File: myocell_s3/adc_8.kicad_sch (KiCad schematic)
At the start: 50 parts, among them U2 ADS1298xPAG

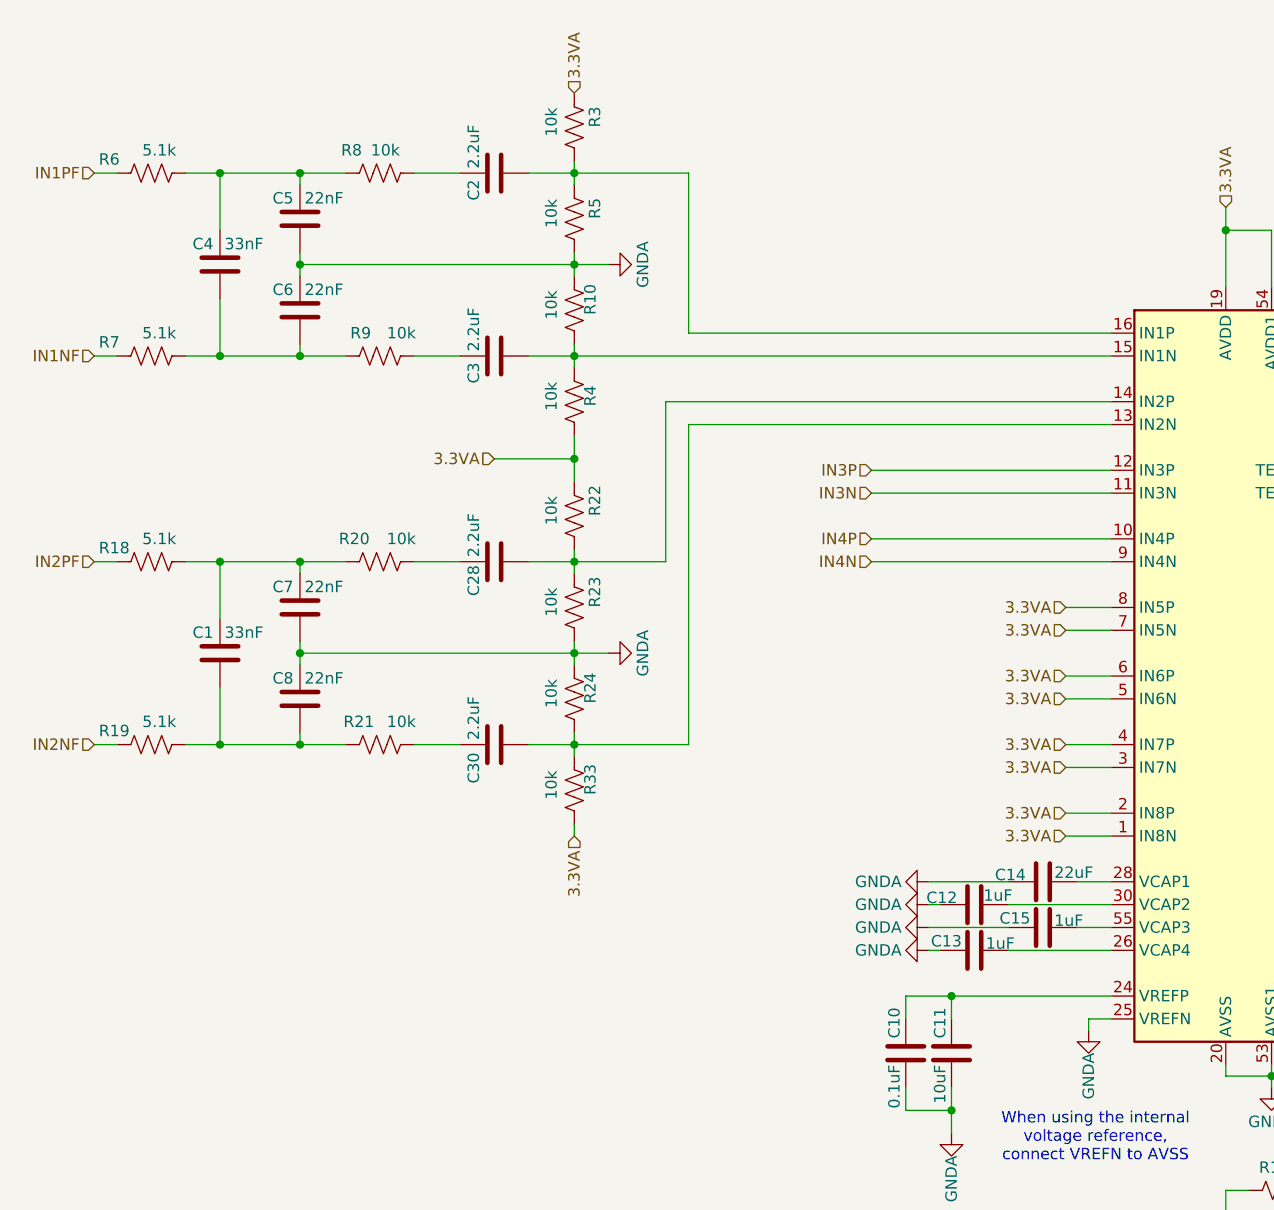
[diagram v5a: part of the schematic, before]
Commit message: schematic updated: channels 3,4 is onboard now
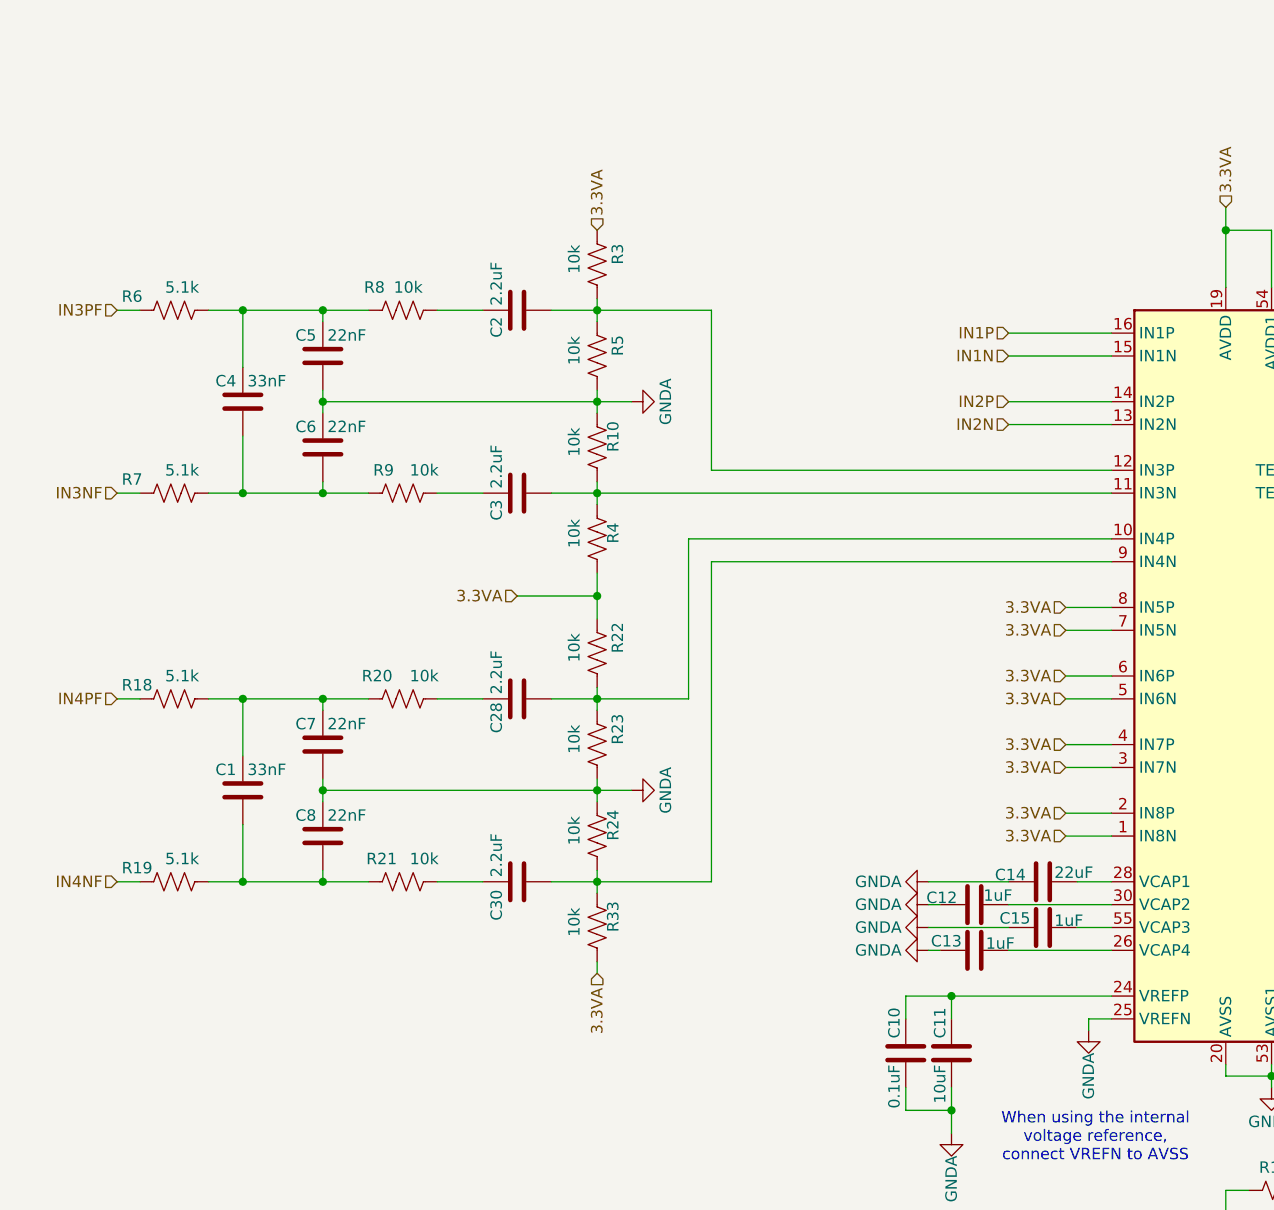
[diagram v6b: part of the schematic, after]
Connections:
- net IN3N is gone; now on an unnamed net: U2.11 (IN3N)
- net IN3P is gone; now on an unnamed net: U2.12 (IN3P)
- net IN4N is gone; now on an unnamed net: U2.9 (IN4N)
- net IN4P is gone; now on an unnamed net: U2.10 (IN4P)
- net at C3.2, R10.1, R4.2: no longer U2.15 (IN1N)
- net at C28.2, R22.1, R23.2: no longer U2.14 (IN2P)
- net at C2.2, R3.1, R5.2: no longer U2.16 (IN1P)
- net at C30.2, R24.1, R33.2: no longer U2.13 (IN2N)
- net IN1NF renamed IN3NF
- net IN1PF renamed IN3PF
- net IN2NF renamed IN4NF
- net IN2PF renamed IN4PF
- new net IN1N: U2.15 (IN1N)
- new net IN1P: U2.16 (IN1P)
- new net IN2N: U2.13 (IN2N)
- new net IN2P: U2.14 (IN2P)
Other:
- moved on the sheet: C1, C2, C28, C3, C30, C4, C5, C6, C7, C8, R10, R18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

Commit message: tracing analogue interfaces
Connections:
- net in3-: now reaches C3.2, R10.1, R4.2, U2.11 (IN3N)
- net in4+: now reaches C28.2, R22.1, R23.2, U2.10 (IN4P)
- net in3+: now reaches C2.2, R3.1, R5.2, U2.12 (IN3P)
- net in4-: now reaches C30.2, R24.1, R33.2, U2.9 (IN4N)
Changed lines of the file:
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@@
+		)
+	)
+	(label "in4+"
+		(at 115.57 73.66 0)
+		(effects
+			(font
+				(size 1.27 1.27)
+			)
+			(justify left bottom)
+		)
+	)
+	(label "in2-"
+		(at 135.89 60.96 0)
+		(effects
+			(font
+				(size 1.27 1.27)
+			)
+			(justify left bottom)
+		)
+	)
+	(label "in1-"
+		(at 135.89 53.34 0)
+		(effects
+			(font
+				(size 1.27 1.27)
+			)
+			(justify left bottom)
+		)
+	)
+	(label "in3+"
+		(at 115.57 66.04 0)
+		(effects
+			(font
+				(size 1.27 1.27)
+			)
+			(justify left bottom)
+		)
+	)
+	(label "in4-"
+		(at 115.57 76.2 0)
+		(effects
+			(font
+				(size 1.27 1.27)
+			)
+			(justify left bottom)
+		)
+	)
+	(label "in3-"
+		(at 115.57 68.58 0)
+		(effects
+			(font
+				(size 1.27 1.27)
+			)
+			(justify left bottom)
+		)
+	)
+	(label "in1+"
+		(at 135.89 50.8 0)
+		(effects
+			(font
+				(size 1.27 1.27)
+			)
+			(justify left bottom)
+		)
+	)
+	(label "in2+"
+		(at 135.89 58.42 0)
+		(effects
+			(font
+				(size 1.27 1.27)
+			)
+			(justify left bottom)
 		)
 	)

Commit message: tracing polygons
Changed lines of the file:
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@@
 	(wire
 		(pts
-			(xy 31.75 111.76) (xy 34.29 111.76)
+			(xy 25.4 111.76) (xy 34.29 111.76)
 		)
 		(stroke
@@
 	(wire
 		(pts
-			(xy 31.75 91.44) (xy 34.29 91.44)
+			(xy 25.4 91.44) (xy 34.29 91.44)
 		)
 		(stroke
@@
 	(wire
 		(pts
-			(xy 31.75 48.26) (xy 34.29 48.26)
+			(xy 24.13 48.26) (xy 34.29 48.26)
 		)
 		(stroke
@@
 	(wire
 		(pts
-			(xy 31.75 68.58) (xy 34.29 68.58)
+			(xy 24.13 68.58) (xy 34.29 68.58)
 		)
 		(stroke
@@
 			(width 0)
 			(type default)
+		)
+	)
+	(label "in3f-"
+		(at 26.67 68.58 0)
+		(effects
+			(font
+				(size 1.27 1.27)
+			)
+			(justify left bottom)
 		)
 	)
@@
 		)
 	)
+	(label "in3f+"
+		(at 26.67 48.26 0)
+		(effects
+			(font
+				(size 1.27 1.27)
+			)
+			(justify left bottom)
+		)
+	)
 	(label "in1-"
 		(at 135.89 53.34 0)
@@
 		)
 	)
+	(label "in4f+"
+		(at 26.67 91.44 0)
+		(effects
+			(font
+				(size 1.27 1.27)
+			)
+			(justify left bottom)
+		)
+	)
 	(label "in1+"
 		(at 135.89 50.8 0)
+		(effects
+			(font
+				(size 1.27 1.27)
+			)
+			(justify left bottom)
+		)
+	)
+	(label "in4f-"
+		(at 26.67 111.76 0)
 		(effects
 			(font
@@
 	(hierarchical_label "IN3PF"
 		(shape input)
-		(at 31.75 48.26 180)
+		(at 24.13 48.26 180)
 		(effects
 			(font
@@
 	(hierarchical_label "IN3NF"
 		(shape input)
-		(at 31.75 68.58 180)
+		(at 24.13 68.58 180)
 		(effects
 			(font
@@
 	(hierarchical_label "IN4NF"
 		(shape input)
-		(at 31.75 111.76 180)
+		(at 25.4 111.76 180)
 		(effects
 			(font
@@
 	(hierarchical_label "IN4PF"
 		(shape input)
-		(at 31.75 91.44 180)
-		(effects
-			(font
+		(at 25.4 91.44 180)
+		(effects
+			(font
